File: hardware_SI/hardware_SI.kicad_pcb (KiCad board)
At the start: 2 copper layers, 228 x 147.6 mm, 58 parts, among them J1 Barrel_Jack_Switch, J2 Conn_01x07_Female, J3 USB_B_Micro, Q1 SI2323DS-T1, Q2 SI2323DS-T1, SW1 SW_SPDT, U1 OMEGA2+, U2 LTC4085EDEPBF, U3 TPS61200DRC, U4 LD1117S33TR_SOT223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

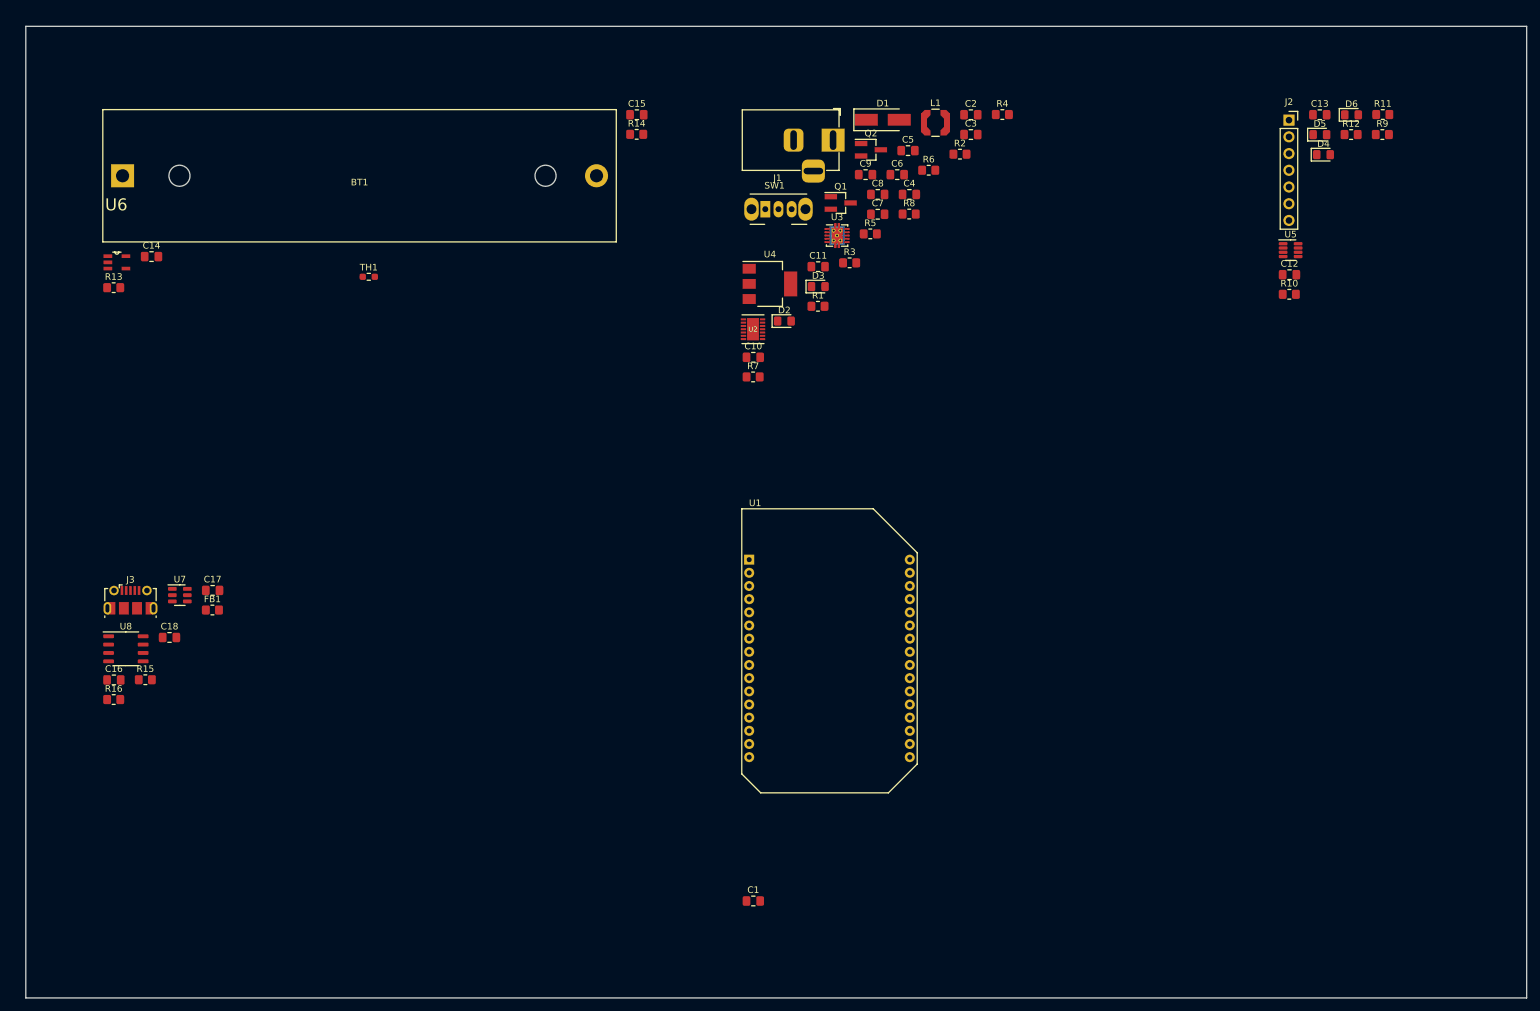
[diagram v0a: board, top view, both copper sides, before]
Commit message: Ubicación componentes PCB
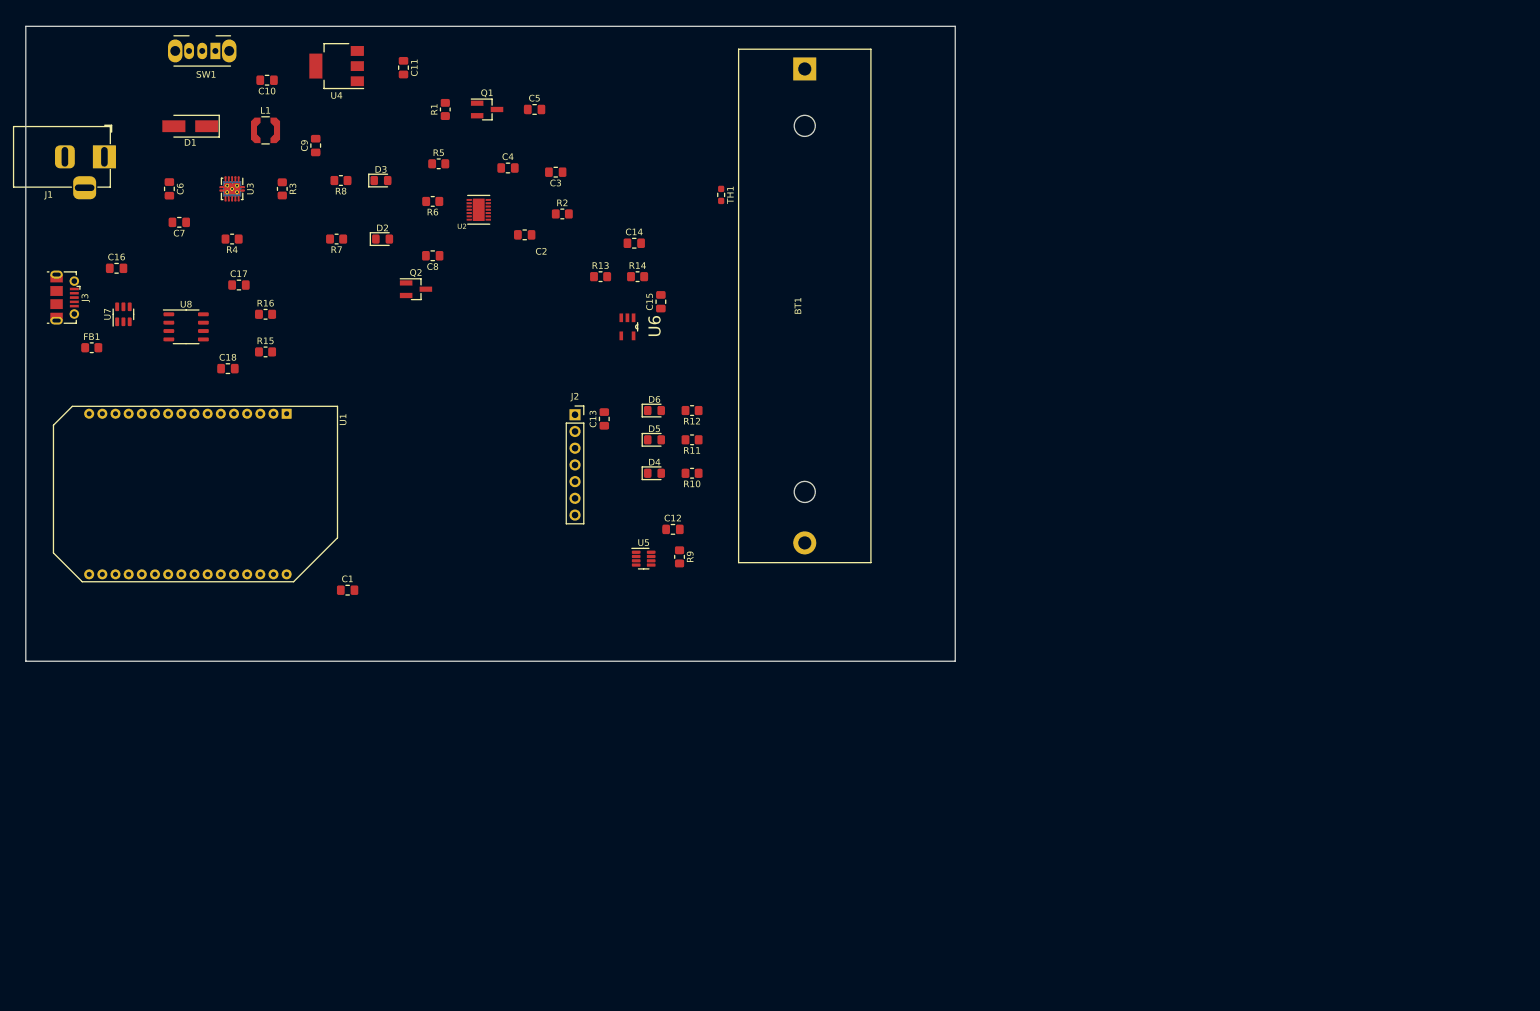
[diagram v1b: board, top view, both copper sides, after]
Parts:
- moved R9 124.6 mm to (146.7, 104.8), turned to -90 degrees
- moved R4 118.5 mm to (78.7, 56.5), turned to 180 degrees
- moved C13 118.1 mm to (135.3, 83.8), turned to 90 degrees
- moved J2 117.3 mm to (130.8, 83.2)
- moved R11 116.0 mm to (148.6, 87.0), turned to 180 degrees
- moved D6 115.0 mm to (142.9, 82.6)
- moved D4 112.6 mm to (142.9, 92.1)
- moved D5 111.2 mm to (142.9, 87.0)
- moved J1 110.7 mm to (59.3, 44.0)
- moved C6 110.6 mm to (69.2, 48.9), turned to -90 degrees
- moved U5 108.9 mm to (141.3, 105.1)
- moved R12 108.5 mm to (148.6, 82.6), turned to 180 degrees
- moved C7 106.1 mm to (70.7, 54.0), turned to 180 degrees
- moved D1 105.2 mm to (72.4, 39.4), turned to 180 degrees
- moved BT1 104.9 mm to (165.7, 30.7), turned to -90 degrees
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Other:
- board size 228 x 147.6 mm -> 141.2 x 96.5 mm

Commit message: Diseño PCB
No estoy seguro si los huecos de los tornillos se hacen así jaja
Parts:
- added ?: , , F.Cu at (52.1, 26.7)
- added ?: , , F.Cu at (52.1, 114.3)
- added REF**: MountingHole_2.2mm_M2_Pad, MountingHole:MountingHole_2.2mm_M2_Pad, F.Cu at (52.1, 114.3)
- added REF**: MountingHole_2.2mm_M2_Pad, MountingHole:MountingHole_2.2mm_M2_Pad, F.Cu at (52.1, 26.7)
- added REF**: MountingHole_2.2mm_M2_Pad, MountingHole:MountingHole_2.2mm_M2_Pad, F.Cu at (149.9, 114.3)
- added REF**: MountingHole_2.2mm_M2_Pad, MountingHole:MountingHole_2.2mm_M2_Pad, F.Cu at (149.9, 26.7)
- BT1, TH1: moved to B.Cu
- moved TH1 33.6 mm to (127.0, 71.1)
- moved C9 28.5 mm to (69.8, 61.0)
- moved BT1 26.5 mm to (139.7, 35.6)
- moved U5 24.8 mm to (116.8, 109.2)
- moved FB1 22.7 mm to (73.7, 57.1)
- moved R9 22.7 mm to (124.5, 109.2)
- moved C12 19.0 mm to (127.0, 104.1)
- moved C16 15.2 mm to (76.2, 63.5), turned to 180 degrees
- moved D1 12.5 mm to (60.3, 36.2)
- moved L1 12.3 mm to (71.8, 37.5)
- moved C10 10.9 mm to (93.3, 38.1), turned to 0 degrees
- moved C13 8.85 mm to (130.8, 76.2)
- moved R10 5.27 mm to (144.4, 95.2)
- moved R11 5.27 mm to (144.4, 90.2)
- moved R12 5.27 mm to (144.4, 85.7)
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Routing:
- net +3V3: track 0.00 -> 249.9 mm
- net +5VL: track 0.00 -> 132.0 mm, vias 0 -> 2
- net /RST_W: track 0.00 -> 131.8 mm, vias 0 -> 2
- net /SDA: track 0.00 -> 115.2 mm, vias 0 -> 1
- net +5VP: track 0.00 -> 113.5 mm, vias 0 -> 4
- net +5VA: track 0.00 -> 113.1 mm, vias 0 -> 2
- net /IO19: track 0.00 -> 109.2 mm, vias 0 -> 1
- net /SCL: track 0.00 -> 108.0 mm, vias 0 -> 1
- net /IO15: track 0.00 -> 79.7 mm, vias 0 -> 1
- net +BATT: track 0.00 -> 74.9 mm, vias 0 -> 1
- net /D/C: track 0.00 -> 74.6 mm, vias 0 -> 1
- net /IO16: track 0.00 -> 74.1 mm, vias 0 -> 1
- net /RST_OLED: track 0.00 -> 72.8 mm
- net /CS1: track 0.00 -> 72.8 mm, vias 0 -> 2
- net /SPI_CLK: track 0.00 -> 71.3 mm, vias 0 -> 1
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- added copper zone on B.Cu, net GND
- added copper zone on F.Cu, net GND
- added copper zone on F.Cu, net GNDPWR
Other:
- board size 141.2 x 96.5 mm -> 106.7 x 95.9 mm
